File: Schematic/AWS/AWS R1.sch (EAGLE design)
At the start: 23 parts, among them U1 SN754410_NE_16

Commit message: Modified Board
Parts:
- added U$3: PTC, GeekAmmo:PTC
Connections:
- new net N$4: J4.1, U$3.2
- net 12V: now also U$3.1; no longer J4.1
- net 5V: now also J6.2; no longer J6.1
- net GND: now also J3.2, J6.1; no longer J3.1, J6.2
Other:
- moved on the sheet: J4
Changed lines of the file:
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@@
 <part name="R8" library="SparkFun-Resistors" deviceset="RESISTOR" device="PTH-1/4W" value="330"/>
 <part name="U$2" library="GeekAmmo" deviceset="DOCFIELD1" device=""/>
+<part name="U$3" library="GeekAmmo" deviceset="PTC" device=""/>
 </parts>
 <sheets>
@@
 <instance part="J2" gate="G$1" x="0" y="91.44" rot="R180"/>
 <instance part="J3" gate="G$1" x="0" y="78.74" rot="R180"/>
-<instance part="J4" gate="G$1" x="-68.58" y="139.7" rot="R270"/>
+<instance part="J4" gate="G$1" x="-68.58" y="144.78" rot="R270"/>
 <instance part="J5" gate="G$1" x="-53.34" y="139.7" rot="R270"/>
 <instance part="J6" gate="G$1" x="-35.56" y="139.7" rot="R270"/>
@@
 <instance part="R8" gate="G$1" x="-22.86" y="35.56" rot="R180"/>
 <instance part="U$2" gate="G$1" x="66.04" y="30.48"/>
+<instance part="U$3" gate="G$1" x="-73.66" y="137.16"/>
 </instances>
 <busses>
@@
 </segment>
 <segment>
-<pinref part="J4" gate="G$1" pin="1"/>
 <pinref part="SUPPLY4" gate="G$1" pin="12V"/>
-<wire x1="-68.58" y1="132.08" x2="-78.74" y2="132.08" width="0.1524" layer="91"/>
 <wire x1="-78.74" y1="132.08" x2="-78.74" y2="129.54" width="0.1524" layer="91"/>
 <pinref part="D1" gate="G$1" pin="C"/>
@@
 <wire x1="-73.66" y1="129.54" x2="-78.74" y2="129.54" width="0.1524" layer="91"/>
 <junction x="-78.74" y="129.54"/>
+<pinref part="U$3" gate="G$1" pin="1"/>
+<wire x1="-81.28" y1="137.16" x2="-81.28" y2="132.08" width="0.1524" layer="91"/>
+<wire x1="-81.28" y1="132.08" x2="-78.74" y2="132.08" width="0.1524" layer="91"/>
 </segment>
 <segment>
@@
 <segment>
 <pinref part="J4" gate="G$1" pin="2"/>
-<wire x1="-66.04" y1="132.08" x2="-66.04" y2="129.54" width="0.1524" layer="91"/>
+<wire x1="-66.04" y1="137.16" x2="-66.04" y2="129.54" width="0.1524" layer="91"/>
 <pinref part="GND1" gate="1" pin="GND"/>
 <wire x1="-66.04" y1="129.54" x2="-60.96" y2="129.54" width="0.1524" layer="91"/>
@@
 <wire x1="-50.8" y1="129.54" x2="-43.18" y2="129.54" width="0.1524" layer="91"/>
 <junction x="-50.8" y="129.54"/>
-<pinref part="J6" gate="G$1" pin="2"/>
-<wire x1="-43.18" y1="129.54" x2="-33.02" y2="129.54" width="0.1524" layer="91"/>
-<wire x1="-33.02" y1="129.54" x2="-33.02" y2="132.08" width="0.1524" layer="91"/>
 <pinref part="D2" gate="G$1" pin="A"/>
 <wire x1="-43.18" y1="124.46" x2="-43.18" y2="129.54" width="0.1524" layer="91"/>
+<pinref part="J6" gate="G$1" pin="1"/>
+<wire x1="-43.18" y1="129.54" x2="-35.56" y2="129.54" width="0.1524" layer="91"/>
+<wire x1="-35.56" y1="129.54" x2="-35.56" y2="132.08" width="0.1524" layer="91"/>
 <junction x="-43.18" y="129.54"/>
 </segment>
@@
 </segment>
 <segment>
-<pinref part="J3" gate="G$1" pin="1"/>
 <pinref part="GND5" gate="1" pin="GND"/>
-<wire x1="-7.62" y1="78.74" x2="-30.48" y2="78.74" width="0.1524" layer="91"/>
 <pinref part="R7" gate="G$1" pin="1"/>
+<pinref part="J3" gate="G$1" pin="2"/>
+<wire x1="-7.62" y1="76.2" x2="-22.86" y2="76.2" width="0.1524" layer="91"/>
+<wire x1="-22.86" y1="76.2" x2="-22.86" y2="78.74" width="0.1524" layer="91"/>
+<wire x1="-22.86" y1="78.74" x2="-30.48" y2="78.74" width="0.1524" layer="91"/>
 <junction x="-30.48" y="78.74"/>
 </segment>
@@
 <net name="5V" class="0">
 <segment>
-<pinref part="J6" gate="G$1" pin="1"/>
 <pinref part="SUPPLY5" gate="G$1" pin="5V"/>
-<wire x1="-35.56" y1="132.08" x2="-35.56" y2="124.46" width="0.1524" layer="91"/>
 <pinref part="D2" gate="G$1" pin="C"/>
 <wire x1="-35.56" y1="124.46" x2="-35.56" y2="121.92" width="0.1524" layer="91"/>
 <wire x1="-38.1" y1="124.46" x2="-35.56" y2="124.46" width="0.1524" layer="91"/>
+<pinref part="J6" gate="G$1" pin="2"/>
+<wire x1="-33.02" y1="132.08" x2="-33.02" y2="124.46" width="0.1524" layer="91"/>
+<wire x1="-33.02" y1="124.46" x2="-35.56" y2="124.46" width="0.1524" layer="91"/>
 <junction x="-35.56" y="124.46"/>
 </segment>
@@
 </segment>
 </net>
+<net name="N$4" class="0">
+<segment>
+<pinref part="J4" gate="G$1" pin="1"/>
+<pinref part="U$3" gate="G$1" pin="2"/>
+</segment>
+</net>

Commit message: Moved outside
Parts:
- added J9: (no value), SparkFun-Connectors:M025MM
- R9: value 56k -> 51K
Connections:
- new net D0: J9.2, U$1.D0_RX
- net A6: now also J9.1
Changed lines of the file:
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@@
 <part name="R6" library="SparkFun-Resistors" deviceset="RESISTOR" device="PTH-1/4W" value="10k"/>
 <part name="R7" library="SparkFun-Resistors" deviceset="RESISTOR" device="PTH-1/4W" value="3.3k"/>
-<part name="R9" library="SparkFun-Resistors" deviceset="RESISTOR" device="PTH-1/4W" value="56k"/>
+<part name="R9" library="SparkFun-Resistors" deviceset="RESISTOR" device="PTH-1/4W" value="51K"/>
 <part name="R8" library="SparkFun-Resistors" deviceset="RESISTOR" device="PTH-1/4W" value="330"/>
 <part name="U$2" library="GeekAmmo" deviceset="DOCFIELD1" device=""/>
 <part name="U$3" library="GeekAmmo" deviceset="PTC" device=""/>
+<part name="J9" library="SparkFun-Connectors" deviceset="M02" device="5MM"/>
 </parts>
 <sheets>
@@
 <instance part="U$2" gate="G$1" x="66.04" y="30.48"/>
 <instance part="U$3" gate="G$1" x="-73.66" y="137.16"/>
+<instance part="J9" gate="G$1" x="2.54" y="25.4" rot="R180"/>
 </instances>
 <busses>
@@
 <wire x1="-15.24" y1="53.34" x2="-35.56" y2="53.34" width="0.1524" layer="91"/>
 <label x="-35.56" y="53.34" size="1.778" layer="95"/>
+<pinref part="J9" gate="G$1" pin="1"/>
+<wire x1="-5.08" y1="25.4" x2="-15.24" y2="25.4" width="0.1524" layer="91"/>
+<wire x1="-15.24" y1="25.4" x2="-15.24" y2="45.72" width="0.1524" layer="91"/>
 </segment>
 </net>
@@
 </segment>
 </net>
+<net name="D0" class="0">
+<segment>
+<pinref part="J9" gate="G$1" pin="2"/>
+<wire x1="-5.08" y1="22.86" x2="-35.56" y2="22.86" width="0.1524" layer="91"/>
+<label x="-35.56" y="22.86" size="1.778" layer="95"/>
+</segment>
+<segment>
+<pinref part="U$1" gate="G$1" pin="D0_RX"/>
+<wire x1="-63.5" y1="68.58" x2="-55.88" y2="68.58" width="0.1524" layer="91"/>
+<label x="-58.42" y="68.58" size="1.778" layer="95"/>
+</segment>
+</net>

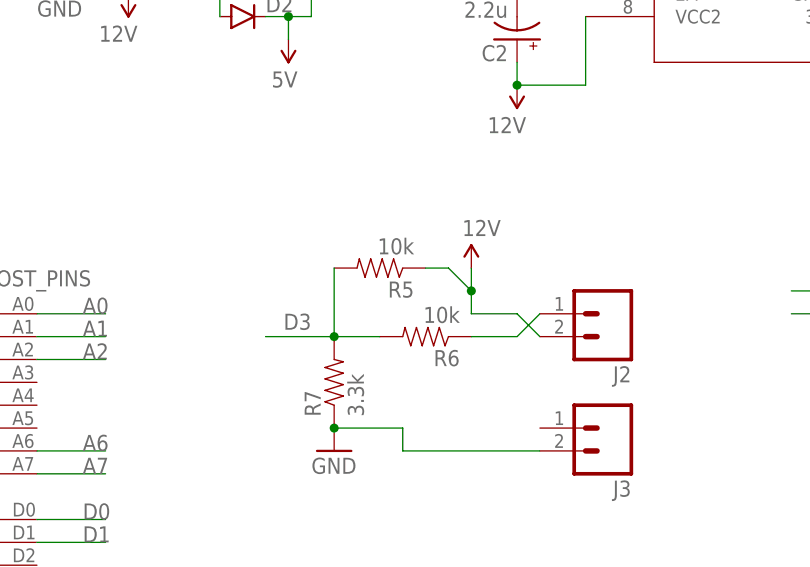
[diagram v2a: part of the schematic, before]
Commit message: Removed 10k pullup on flow sensor
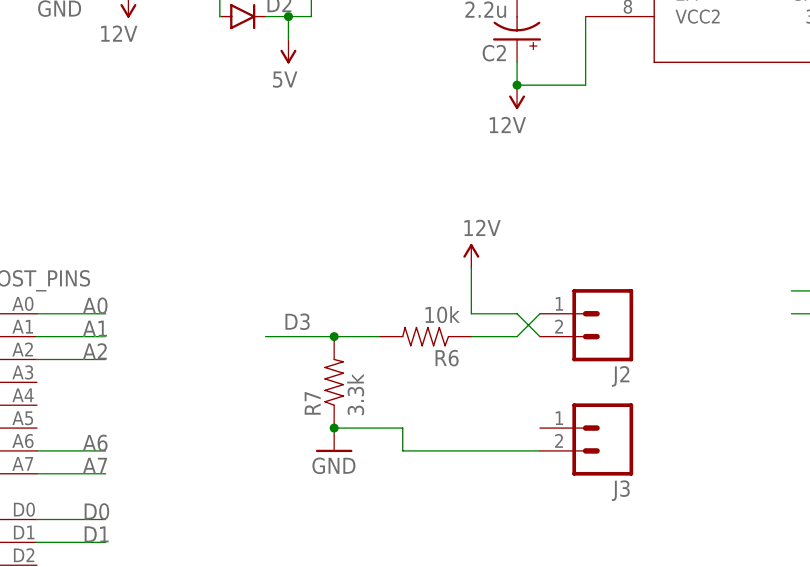
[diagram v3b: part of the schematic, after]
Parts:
- removed R5: 10k, SparkFun-Resistors:RESISTORPTH-1/4W
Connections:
- net 12V: no longer R5.1
- net D3: no longer R5.2
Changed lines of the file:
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@@
 <part name="C1" library="SparkFun-Capacitors" deviceset="CAP_POL" device="PTH1" value="2.2u"/>
 <part name="C2" library="SparkFun-Capacitors" deviceset="CAP_POL" device="PTH1" value="2.2u"/>
-<part name="R5" library="SparkFun-Resistors" deviceset="RESISTOR" device="PTH-1/4W" value="10k"/>
 <part name="R6" library="SparkFun-Resistors" deviceset="RESISTOR" device="PTH-1/4W" value="10k"/>
 <part name="R7" library="SparkFun-Resistors" deviceset="RESISTOR" device="PTH-1/4W" value="3.3k"/>
@@
 <instance part="C1" gate="G$1" x="45.72" y="139.7"/>
 <instance part="C2" gate="G$1" x="-10.16" y="121.92" rot="R180"/>
-<instance part="R5" gate="G$1" x="-25.4" y="96.52" rot="R180"/>
 <instance part="R6" gate="G$1" x="-20.32" y="88.9" rot="R180"/>
 <instance part="R7" gate="G$1" x="-30.48" y="83.82" rot="R90"/>
@@
 <segment>
 <pinref part="SUPPLY9" gate="G$1" pin="12V"/>
-<wire x1="-15.24" y1="91.44" x2="-15.24" y2="93.98" width="0.1524" layer="91"/>
-<pinref part="R5" gate="G$1" pin="1"/>
-<wire x1="-15.24" y1="93.98" x2="-15.24" y2="96.52" width="0.1524" layer="91"/>
-<wire x1="-20.32" y1="96.52" x2="-17.78" y2="96.52" width="0.1524" layer="91"/>
-<wire x1="-17.78" y1="96.52" x2="-15.24" y2="93.98" width="0.1524" layer="91"/>
-<junction x="-15.24" y="93.98"/>
+<wire x1="-15.24" y1="91.44" x2="-15.24" y2="96.52" width="0.1524" layer="91"/>
 <pinref part="J2" gate="G$1" pin="2"/>
 <wire x1="-15.24" y1="91.44" x2="-10.16" y2="91.44" width="0.1524" layer="91"/>
@@
 <pinref part="R6" gate="G$1" pin="2"/>
 <wire x1="-25.4" y1="88.9" x2="-30.48" y2="88.9" width="0.1524" layer="91"/>
-<pinref part="R5" gate="G$1" pin="2"/>
 <wire x1="-30.48" y1="88.9" x2="-38.1" y2="88.9" width="0.1524" layer="91"/>
-<wire x1="-30.48" y1="96.52" x2="-30.48" y2="88.9" width="0.1524" layer="91"/>
 <junction x="-30.48" y="88.9"/>
 <pinref part="R7" gate="G$1" pin="2"/>
